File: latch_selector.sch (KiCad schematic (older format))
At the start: 25 parts, among them SW1 Line Selection, SW3 Step, SW4 Run/Step Mode, U1 74HCT138, U10 LMC555xM, U11 74HCT00, U12 74HCT74, U2 74HCT151, U6 74HCT32

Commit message: changes to stepper circuit, pcb layout changes
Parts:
- removed RN2: 10K, Resistor_THT:R_Array_SIP7, symbol Device:R_Network06
- removed SW3: Step, Button_Switch_THT:SW_NKK_BB15AH, symbol Switch:SW_Push_SPDT
- removed unit 1 of U11
- added C13: 100nF, Capacitor_SMD:C_0805_2012Metric_Pad1.15x1.40mm_HandSolder, symbol Device:C
- added R1: 10K, Resistor_SMD:R_0805_2012Metric_Pad1.15x1.40mm_HandSolder, symbol Device:R_Small
- added RN2: 10K, Resistor_THT:R_Array_SIP5, symbol Device:R_Network04
- added SW3: SW_Push, Button_Switch_THT:SW_PUSH_6mm, symbol Switch:SW_Push
- added unit 4 of U11
- added U13: MAX6816, Package_TO_SOT_SMD:SOT-143, symbol Interface:MAX6816
- RN1: value 270R Bussed -> 1K Bussed; footprint Resistor_THT:R_Array_SIP9 -> Resistor_THT:R_Array_SIP7; symbol Device:R_Network08 -> Device:R_Network06
- U11: footprint Package_DIP:DIP-14_W7.62mm -> (none); MFR Texas Instruments -> (none); MPN CD74HCT00E -> (none); SPN 595-CD74HCT00E -> (none); SPR Mouser -> (none); SPURL https://www.mouser.com/ProductDetail/Texas-Instruments/CD74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 -> (none)
- renumbered C13 to C11, C14 to C12, C11 to C14, C12 to C15, U1 to U4, U2 to U5
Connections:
- net labels removed: RN2_2, RN2_5, RN2_6
- wire segments 116 -> 113
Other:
- moved on the sheet: C14, C15, SW4, U10, U11E, U12A, U12C, U6A, U6B, U6C, U6D, U6E

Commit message: added vias for thermal releaf
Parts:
- U11: footprint (none) -> Package_DIP:DIP-14_W7.62mm
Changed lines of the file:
@@
 F 0 "U11" V 3646 3920 50  0000 R CNN
 F 1 "74HCT00" V 3555 3920 50  0000 R CNN
-F 2 "" H 3600 4100 50  0001 C CNN
+F 2 "Package_DIP:DIP-14_W7.62mm" H 3600 4100 50  0001 C CNN
 F 3 "http://www.ti.com/lit/gpn/sn74hct00" H 3600 4100 50  0001 C CNN
 	2    3600 4100

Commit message: fixed single step, display hookup
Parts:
- removed R1: 10K, Resistor_SMD:R_0805_2012Metric_Pad1.15x1.40mm_HandSolder, symbol Device:R_Small
- RN2: footprint Resistor_THT:R_Array_SIP5 -> Resistor_THT:R_Array_SIP6; symbol Device:R_Network04 -> Device:R_Network05
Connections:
- net labels added: RN2_5, RN2_6
- wire segments 113 -> 112
- no-connect marks 7 -> 6
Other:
- moved on the sheet: C14, C15, SW3, SW4, U10, U11A, U11B, U12A, U13

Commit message: Reorganized board yet again, replaced SMD 555 with TH
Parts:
- removed D1: CMXSH-3 TR, Package_TO_SOT_SMD:SOT-23-6_Handsoldering, symbol Diode:SD103ATW
- removed RN2: 10K, Resistor_THT:R_Array_SIP6, symbol Device:R_Network05
- removed U10: LMC555xM, Package_SO:SOIC-8_3.9x4.9mm_P1.27mm, symbol Timer:LMC555xM
- added D1: CMXSH-3, Package_TO_SOT_SMD:SOT-23-6_Handsoldering, symbol Diode:CMXSH-3
- added R1, R2, R3, R4: 10K, Resistor_SMD:R_0805_2012Metric_Pad1.15x1.40mm_HandSolder, symbol Device:R_Small
- added U14: LMC555xN, Package_DIP:DIP-8_W7.62mm, symbol Timer:LMC555xN
- RN1: value 1K Bussed -> 150R
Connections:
- net labels removed: RN2_1, RN2_3, RN2_4, RN2_5, RN2_6
- wire segments 112 -> 128
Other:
- moved on the sheet: SW4

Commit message: DRC fixed
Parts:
- D1: symbol Diode:CMXSH-3 -> rc2014_monitor-rescue:CMXSH-3-Diode
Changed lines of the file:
@@
 $EndComp
 $Comp
-L Diode:CMXSH-3 D1
+L rc2014_monitor-rescue:CMXSH-3-Diode D1
 U 3 1 5CCA4950
 P 9350 3450
+AR Path="/5CCA4950" Ref="D1"  Part="3"
+AR Path="/5CBDBC11/5CCA4950" Ref="D1"  Part="3"
 F 0 "D1" H 9550 3400 50  0000 C CNN
 F 1 "CMXSH-3" H 9250 3600 50  0000 C CNN
@@
 $EndComp
 $Comp
-L Diode:CMXSH-3 D1
+L rc2014_monitor-rescue:CMXSH-3-Diode D1
 U 2 1 5CCA3189
 P 9350 3350
+AR Path="/5CCA3189" Ref="D1"  Part="2"
+AR Path="/5CBDBC11/5CCA3189" Ref="D1"  Part="2"
 F 0 "D1" H 9550 3300 50  0000 C CNN
 F 1 "CMXSH-3" H 9250 3600 50  0000 C CNN
@@
 $EndComp
 $Comp
-L Diode:CMXSH-3 D1
+L rc2014_monitor-rescue:CMXSH-3-Diode D1
 U 1 1 5CC9FE3A
 P 9350 3250
+AR Path="/5CC9FE3A" Ref="D1"  Part="1"
+AR Path="/5CBDBC11/5CC9FE3A" Ref="D1"  Part="1"
 F 0 "D1" H 9550 3200 50  0000 C CNN
 F 1 "CMXSH-3" H 9250 3600 50  0000 C CNN

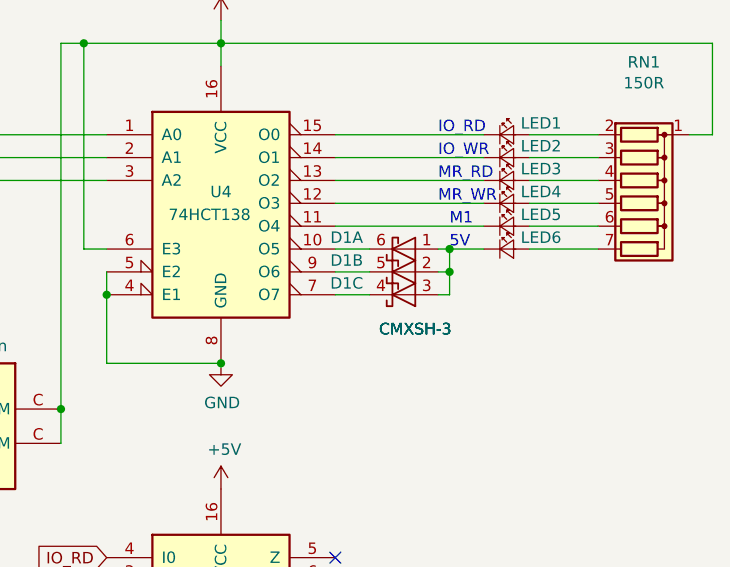
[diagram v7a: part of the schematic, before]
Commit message: replaced diode array with thru-hole
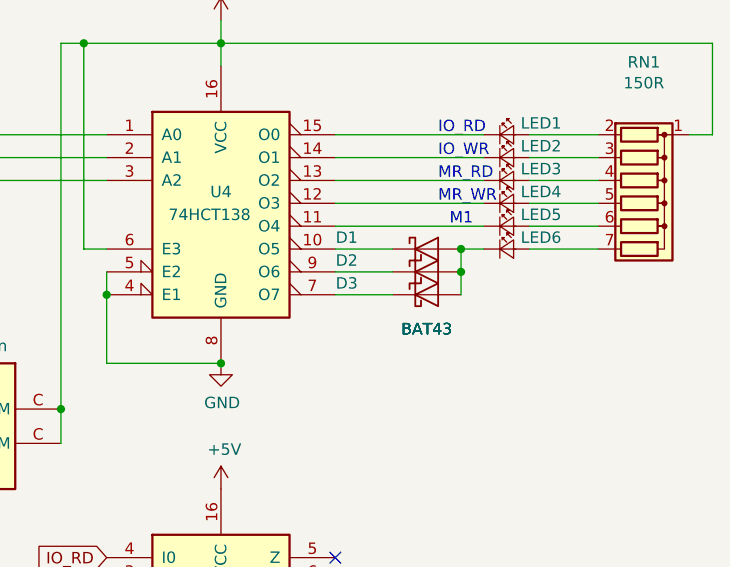
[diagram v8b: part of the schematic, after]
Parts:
- removed D1: CMXSH-3, Package_TO_SOT_SMD:SOT-23-6_Handsoldering, symbol rc2014_monitor-rescue:CMXSH-3-Diode
- added D1, D2, D3: BAT43, Diode_THT:D_DO-35_SOD27_P7.62mm_Horizontal, symbol Diode:BAT43
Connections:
- net at U4.10 (O5): now also D1.1 (K)
- net at U4.7 (O7): now also D3.1 (K)
- net at U4.9 (O6): now also D2.1 (K)
- net at LED6.1 (K): now also D1.2 (A), D2.2 (A), D3.2 (A)
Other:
- note removed: "5V"
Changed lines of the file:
@@
 	7900 2350 8000 2350
 Connection ~ 8000 2350
-Text Notes 9600 3250 0    50   ~ 0
-5V
 $Comp
 L power:GND #PWR?
@@
 	8100 3350 8100 3450
 Connection ~ 8100 3450
-Wire Wire Line
-	9250 3350 9100 3350
-Wire Wire Line
-	9250 3450 9100 3450
 Connection ~ 2100 1150
 Wire Wire Line
@@
 Wire Wire Line
 	2100 1450 2300 1450
-Wire Wire Line
-	9100 3250 9250 3250
-Wire Wire Line
-	9550 3250 9600 3250
-Wire Wire Line
-	9550 3450 9600 3450
-Wire Wire Line
-	9600 3450 9600 3350
-Wire Wire Line
-	9600 3350 9550 3350
-Wire Wire Line
-	9600 3350 9600 3250
-Connection ~ 9600 3350
-Connection ~ 9600 3250
-Wire Wire Line
-	9600 3250 9750 3250
 $Comp
 L Timer:LMC555xN U14
@@
 	1    2200 5200
 	1    0    0    -1
-$EndComp
-$Comp
-L rc2014_monitor-rescue:CMXSH-3-Diode D1
-U 3 1 5CCA4950
-P 9350 3450
-AR Path="/5CCA4950" Ref="D1"  Part="3"
-AR Path="/5CBDBC11/5CCA4950" Ref="D1"  Part="3"
-F 0 "D1" H 9550 3400 50  0000 C CNN
-F 1 "CMXSH-3" H 9250 3600 50  0000 C CNN
-F 2 "Package_TO_SOT_SMD:SOT-23-6_Handsoldering" H 9350 3250 50  0001 C CNN
-F 3 "https://www.diodes.com/assets/Datasheets/ds30374.pdf" H 9300 3450 50  0001 C CNN
-	3    9350 3450
-	-1   0    0    1
-$EndComp
-$Comp
-L rc2014_monitor-rescue:CMXSH-3-Diode D1
-U 2 1 5CCA3189
-P 9350 3350
-AR Path="/5CCA3189" Ref="D1"  Part="2"
-AR Path="/5CBDBC11/5CCA3189" Ref="D1"  Part="2"
-F 0 "D1" H 9550 3300 50  0000 C CNN
-F 1 "CMXSH-3" H 9250 3600 50  0000 C CNN
-F 2 "Package_TO_SOT_SMD:SOT-23-6_Handsoldering" H 9350 3150 50  0001 C CNN
-F 3 "https://www.diodes.com/assets/Datasheets/ds30374.pdf" H 9300 3350 50  0001 C CNN
-	2    9350 3350
-	-1   0    0    1
-$EndComp
-$Comp
-L rc2014_monitor-rescue:CMXSH-3-Diode D1
-U 1 1 5CC9FE3A
-P 9350 3250
-AR Path="/5CC9FE3A" Ref="D1"  Part="1"
-AR Path="/5CBDBC11/5CC9FE3A" Ref="D1"  Part="1"
-F 0 "D1" H 9550 3200 50  0000 C CNN
-F 1 "CMXSH-3" H 9250 3600 50  0000 C CNN
-F 2 "Package_TO_SOT_SMD:SOT-23-6_Handsoldering" H 9350 3050 50  0001 C CNN
-F 3 "https://www.diodes.com/assets/Datasheets/ds30374.pdf" H 9300 3250 50  0001 C CNN
-	1    9350 3250
-	-1   0    0    1
 $EndComp
 $Comp
@@
 	0    -1   -1   0
 $EndComp
+$Comp
+L Diode:BAT43 D2
+U 1 1 5CC85B65
+P 9500 3350
+F 0 "D2" H 9150 3400 50  0000 C CNN
+F 1 "BAT43" H 9500 3100 50  0000 C CNN
+F 2 "Diode_THT:D_DO-35_SOD27_P7.62mm_Horizontal" H 9500 3175 50  0001 C CNN
+F 3 "http://www.vishay.com/docs/85660/bat42.pdf" H 9500 3350 50  0001 C CNN
+	1    9500 3350
+	1    0    0    -1
+$EndComp
+$Comp
+L Diode:BAT43 D1
+U 1 1 5CC88CC1
+P 9500 3250
+F 0 "D1" H 9150 3300 50  0000 C CNN
+F 1 "BAT43" H 9500 2900 50  0000 C CNN
+F 2 "Diode_THT:D_DO-35_SOD27_P7.62mm_Horizontal" H 9500 3075 50  0001 C CNN
+F 3 "http://www.vishay.com/docs/85660/bat42.pdf" H 9500 3250 50  0001 C CNN
+	1    9500 3250
+	1    0    0    -1
+$EndComp
+$Comp
+L Diode:BAT43 D3
+U 1 1 5CC89ED5
+P 9500 3450
+F 0 "D3" H 9150 3500 50  0000 C CNN
+F 1 "BAT43" H 9500 3300 50  0000 C CNN
+F 2 "Diode_THT:D_DO-35_SOD27_P7.62mm_Horizontal" H 9500 3275 50  0001 C CNN
+F 3 "http://www.vishay.com/docs/85660/bat42.pdf" H 9500 3450 50  0001 C CNN
+	1    9500 3450
+	1    0    0    -1
+$EndComp
+Wire Wire Line
+	9100 3250 9350 3250
+Wire Wire Line
+	9100 3350 9350 3350
+Wire Wire Line
+	9100 3450 9350 3450
+Wire Wire Line
+	9650 3450 9650 3350
+Wire Wire Line
+	9750 3250 9650 3250
+Wire Wire Line
+	9650 3350 9650 3250
+Connection ~ 9650 3350
+Connection ~ 9650 3250
 $EndSCHEMATC
